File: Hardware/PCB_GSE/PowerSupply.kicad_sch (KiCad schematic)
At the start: 54 parts, among them J2 Vin_XT30PW-F, U2 LM2673SX-12_NOPB, U3 MPQ9843GLE-5-AEC1-Z, U4 TLV75733PDBVR

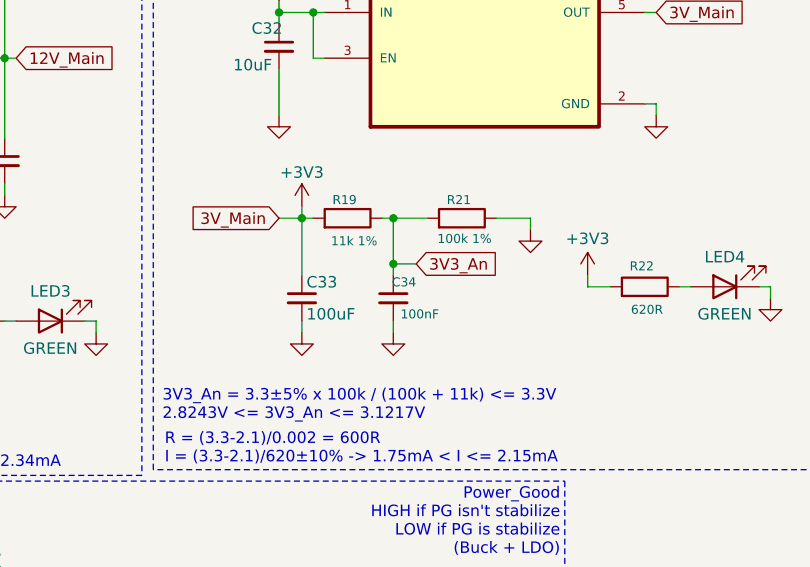
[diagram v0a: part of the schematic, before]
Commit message: fix: decoupling 3v3 missing
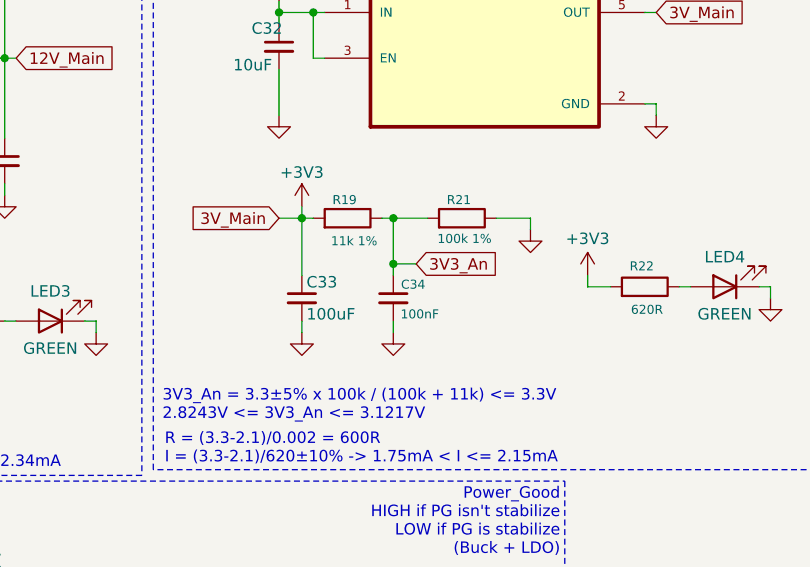
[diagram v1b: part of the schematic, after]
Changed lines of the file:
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@@
 		(dnp no)
 		(property "Reference" "C34"
-			(at 158.75 103.632 0)
+			(at 159.766 103.886 0)
 			(effects
 				(font

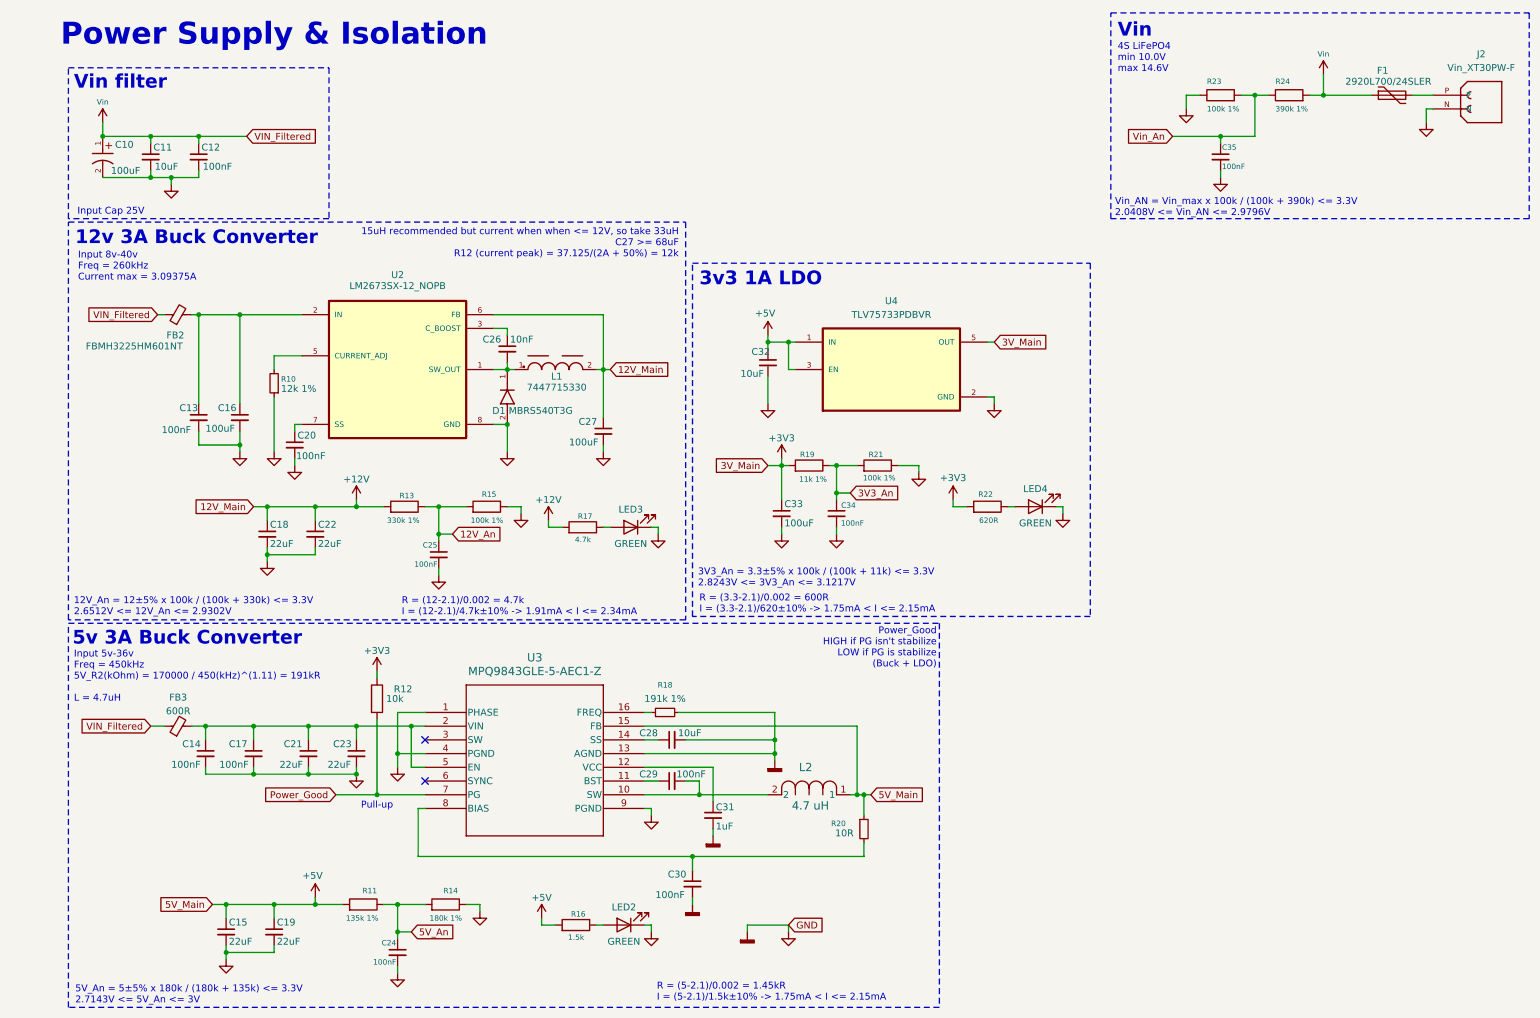
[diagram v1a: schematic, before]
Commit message: wip : Reduce BOM and fill all datasheet, digikey and MPN
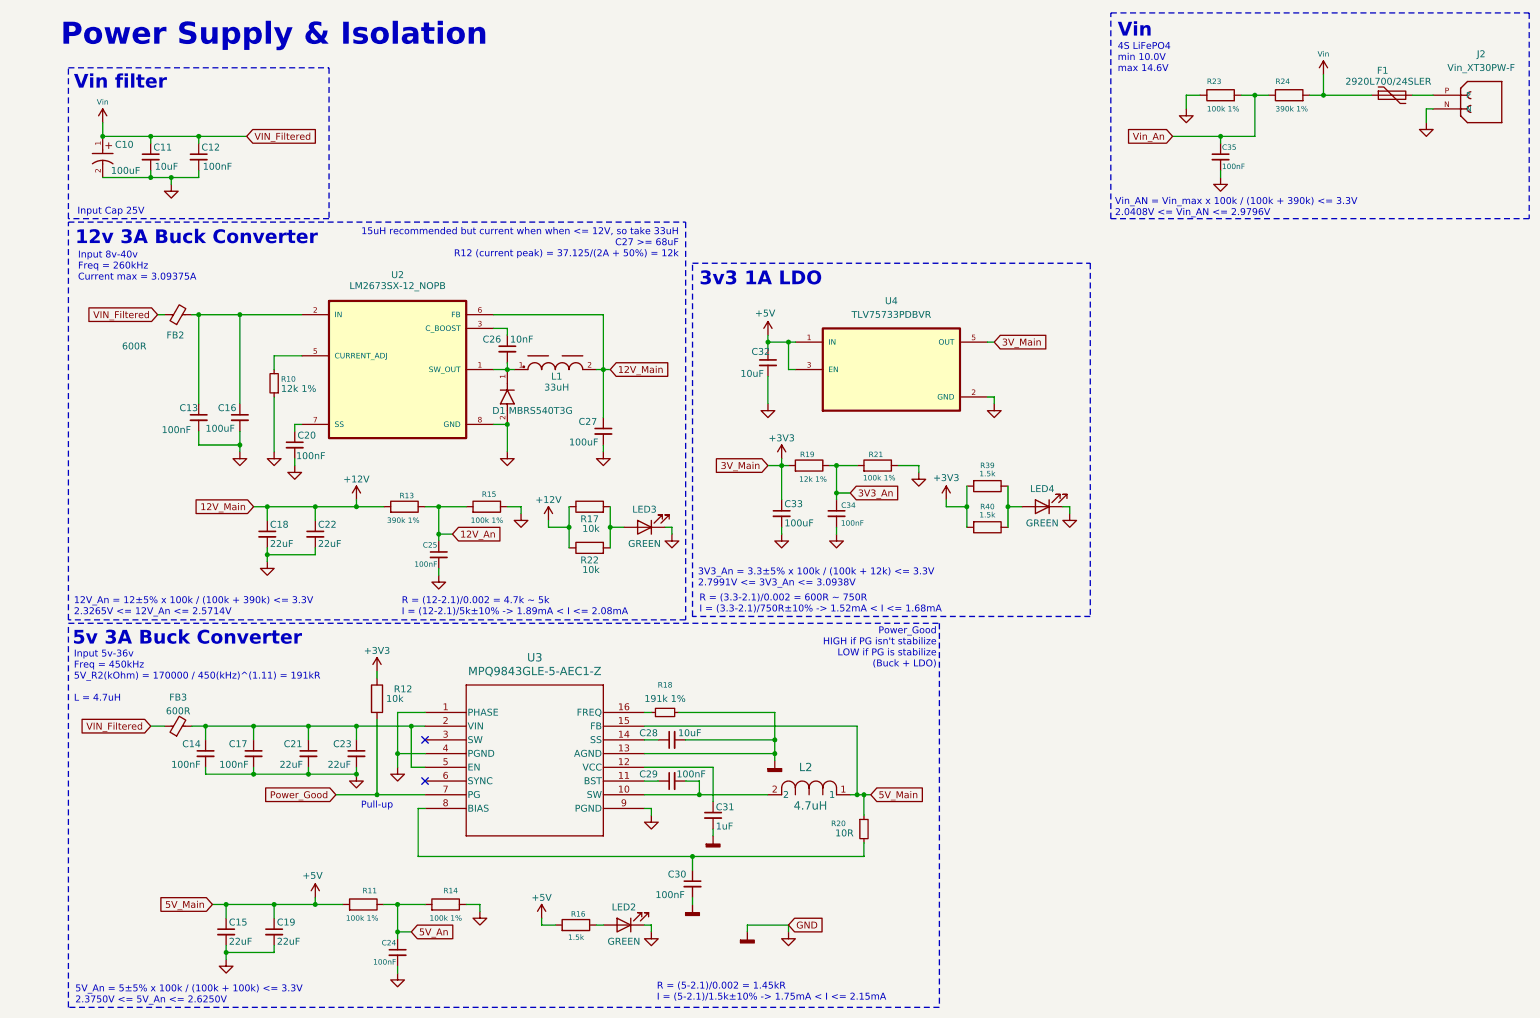
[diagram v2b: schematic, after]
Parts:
- added R39, R40: 1.5k, Resistor_SMD:R_0805_2012Metric, symbol Device:R
- C10: footprint Capacitor_THT:CP_Radial_D6.3mm_P2.50mm -> PCB_GSE:U2-K_NCH; DigiKey_Part_Number (none) -> 493-3937-1-ND; Manufacturer_Part_Number (none) -> UCL1E101MCL1GS
- C11, C32: DigiKey_Part_Number (none) -> 1276-2891-1-ND; Manufacturer_Part_Number (none) -> CL21A106KAYNNNE
- C12, C13, C20: footprint Capacitor_SMD:C_0805_2012Metric -> Capacitor_SMD:C_0603_1608Metric; DigiKey_Part_Number (none) -> 399-C0603C104K3RACTUCT-ND; Manufacturer_Part_Number (none) -> C0603C104K3RACTU
- C14, C17, C24, C25, C29, C30, C34, C35: footprint ODB:C_0402_1005Metric -> Capacitor_SMD:C_0603_1608Metric; DigiKey_Part_Number 311-3342-1-ND -> 399-C0603C104K3RACTUCT-ND; Manufacturer_Part_Number CC0402KRX5R9BB104 -> C0603C104K3RACTU
- C16, C27: footprint Capacitor_SMD:C_0805_2012Metric -> Capacitor_SMD:C_1210_3225Metric; DigiKey_Part_Number (none) -> 587-5426-1-ND; Manufacturer_Part_Number (none) -> EMK325ABJ107MM-P
- C26: DigiKey_Part_Number (none) -> 1276-2434-1-ND; Manufacturer_Part_Number (none) -> CL21B103KAANNNC
- C28: footprint Capacitor_SMD:C_0603_1608Metric -> Capacitor_SMD:C_0805_2012Metric; DigiKey_Part_Number 490-13248-1-ND -> 1276-2891-1-ND; Manufacturer_Part_Number GRM188R6YA106MA73D -> CL21A106KAYNNNE
- C31: footprint Capacitor_SMD:C_0603_1608Metric -> Capacitor_SMD:C_0805_2012Metric
- C33: footprint Capacitor_SMD:C_0805_2012Metric -> Capacitor_SMD:C_1210_3225Metric; DigiKey_Part_Number 445-14428-1-ND -> 587-5426-1-ND; Manufacturer_Part_Number C2012X5R1V226M125AC -> EMK325ABJ107MM-P
- D1: footprint MBRS540T3G:DIOM7959X261N -> pcb_moteur:DIODE_SMB_2L_ONS; DigiKey_Part_Number MBRS540T3GOSCT-ND -> MBRS130LT3GOSCT-ND; Manufacturer_Part_Number (none) -> MBRS130LT3G
- FB2: value FBMH3225HM601NT -> 600R; DigiKey_Part_Number (none) -> 587-1755-1-ND; Manufacturer_Part_Number (none) -> FBMH3225HM601NT
- J2: footprint (none) -> pcb_moteur:XT30PW-F; DigiKey_Part_Number (none) -> -
- L1: value 7447715330 -> 33uH; footprint WE-PD_1245:WE-PD_1245 -> pcb_moteur:WE-PD_1245; DigiKey_Part_Number (none) -> 732-2196-1-ND; Manufacturer_Part_Number (none) -> 7447715330
- L2: value 4.7 uH -> 4.7uH; footprint ODB:IND_PA4342_PUL -> pcb_moteur:IND_PA4342_PUL
- LED2, LED3: footprint ODB:LED_QBLP601-AG15 -> pcb_moteur:LED_QBLP601-AG15
- R10: footprint Resistor_SMD:R_0603_1608Metric -> Resistor_SMD:R_0805_2012Metric; DigiKey_Part_Number P191KDBCT-ND -> 311-12.0KCRCT-ND; Manufacturer_Part_Number ERA-3AEB1913V -> RC0805FR-0712KL
- R11: value 135k 1% -> 100k 1%; footprint Resistor_SMD:R_0603_1608Metric -> Resistor_SMD:R_0805_2012Metric; DigiKey_Part_Number 13-RT0603BRD07135KLCT-ND -> 311-100KCRCT-ND; Manufacturer_Part_Number RT0603BRD07135KL -> RC0805FR-07100KL
- R12, R18: footprint Resistor_SMD:R_0603_1608Metric -> Resistor_SMD:R_0805_2012Metric
- R13: value 330k 1% -> 390k 1%; footprint Resistor_SMD:R_0603_1608Metric -> Resistor_SMD:R_0805_2012Metric; DigiKey_Part_Number 13-RT0603BRD07135KLCT-ND -> 2019-RK73H2ATTD3903FCT-ND; Manufacturer_Part_Number RT0603BRD07135KL -> RK73H2ATTD3903F
- R14: value 180k 1% -> 100k 1%; footprint Resistor_SMD:R_0603_1608Metric -> Resistor_SMD:R_0805_2012Metric; DigiKey_Part_Number P180KDBCT-ND -> 311-100KCRCT-ND; Manufacturer_Part_Number ERA-3AEB184V -> RC0805FR-07100KL
- R15, R21: footprint Resistor_SMD:R_0603_1608Metric -> Resistor_SMD:R_0805_2012Metric; DigiKey_Part_Number P180KDBCT-ND -> 311-100KCRCT-ND; Manufacturer_Part_Number ERA-3AEB184V -> RC0805FR-07100KL
- R16: footprint Resistor_SMD:R_0603_1608Metric -> Resistor_SMD:R_0805_2012Metric; DigiKey_Part_Number 408-1766-1-ND -> P1.5KDBCT-ND; Manufacturer_Part_Number URG1608L-152-L-T05 -> ERA-3AEB152V
- R17: value 4.7k -> 10k; footprint Resistor_SMD:R_0603_1608Metric -> Resistor_SMD:R_0805_2012Metric; DigiKey_Part_Number 408-1766-1-ND -> 311-10.0KHRCT-ND; Manufacturer_Part_Number URG1608L-152-L-T05 -> RC0603FR-0710KL
- R19: value 11k 1% -> 12k 1%; footprint Resistor_SMD:R_0603_1608Metric -> Resistor_SMD:R_0805_2012Metric; DigiKey_Part_Number 13-RT0603BRD07135KLCT-ND -> 311-12.0KCRCT-ND; Manufacturer_Part_Number RT0603BRD07135KL -> RC0805FR-0712KL
- R20: footprint ODB:R_0402_1005Metric -> Resistor_SMD:R_0805_2012Metric
- R22: value 620R -> 10k; DigiKey_Part_Number (none) -> 311-10.0KHRCT-ND; Manufacturer_Part_Number (none) -> RC0603FR-0710KL
- R23: footprint Resistor_SMD:R_0603_1608Metric -> Resistor_SMD:R_0805_2012Metric; DigiKey_Part_Number RG16P27.0KBCT-ND -> 311-100KCRCT-ND; Manufacturer_Part_Number RG1608P-273-B-T5 -> RC0805FR-07100KL
- R24: footprint Resistor_SMD:R_0603_1608Metric -> Resistor_SMD:R_0805_2012Metric; DigiKey_Part_Number P180KDBCT-ND -> 2019-RK73H2ATTD3903FCT-ND; Manufacturer_Part_Number ERA-3AEB184V -> RK73H2ATTD3903F
- U2: footprint LM2673SX-12_NOPB:TO127P1435X464-8N -> PCB_GSE:LM2673SX-12_NOPB; Manufacturer_Part_Number (none) -> LM2673SX-12/NOPB
- U3: footprint Snapeda:QFN-16__MPQ9843 -> pcb_moteur:MPQ9843GLE_5_AEC1_Z; Manufacturer_Part_Number (none) -> MPQ9843GLE-5-AEC1-Z; Manufacturer_Part_Number  MPQ9843GLE-5-AEC1-Z -> (none)
- U4: footprint TLV75733PDBVR:SOT95P280X145-5N -> Package_TO_SOT_SMD:SOT-23-5; Manufacturer_Part_Number (none) -> TLV75733PDBVR
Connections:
- net +12V: now also R17.1, R22.1; no longer R17.2
- net +3V3: now also R39.2, R40.2; no longer R22.2
- net at LED4.2 (A): now also R39.1, R40.1; no longer R22.1
- net at LED3.2 (A): now also R17.2, R22.2; no longer R17.1
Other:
- note added: "12V_An = 12±5% x 100k / (100k + 390k) <= 3.3V 2.3265V <= 12V_An <= 2.5714V"
- note added: "3V3_An = 3.3±5% x 100k / (100k + 12k) <= 3.3V 2.7991V <= 3V3_An <= 3.0938V"
- note added: "5V_An = 5±5% x 100k / (100k + 100k) <= 3.3V 2.3750V <= 5V_An <= 2.6250V"
- note added: "R = (12-2.1)/0.002 = 4.7k ~ 5k I = (12-2.1)/5k±10% -> 1.89mA < I <= 2.08mA"
- note added: "R = (3.3-2.1)/0.002 = 600R ~ 750R I = (3.3-2.1)/750R±10% -> 1.52mA < I <= 1.68mA"
- note removed: "12V_An = 12±5% x 100k / (100k + 330k) <= 3.3V 2.6512V <= 12V_An <= 2.9302V"
- note removed: "3V3_An = 3.3±5% x 100k / (100k + 11k) <= 3.3V 2.8243V <= 3V3_An <= 3.1217V"
- note removed: "5V_An = 5±5% x 180k / (180k + 135k) <= 3.3V 2.7143V <= 5V_An <= 3V"
- note removed: "R = (12-2.1)/0.002 = 4.7k I = (12-2.1)/4.7k±10% -> 1.91mA < I <= 2.34mA"
- note removed: "R = (3.3-2.1)/0.002 = 600R I = (3.3-2.1)/620±10% -> 1.75mA < I <= 2.15mA"
- moved on the sheet: LED3, LED4

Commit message: wip: begining layout
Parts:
- renumbered R10 to R11, R11 to R12, R12 to R13, R13 to R14, R14 to R15, R15 to R16, R16 to R17, R17 to R18, R22 to R19, R18 to R20, R19 to R21, R20 to R22, R21 to R23, R39 to R24, R40 to R25, R23 to R26, R24 to R27
